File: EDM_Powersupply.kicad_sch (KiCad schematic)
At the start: 19 parts, among them Q1 IPW65R037C6, U1 L7805, U2 STGAP2SM, U3 RP2040, U4 L7815

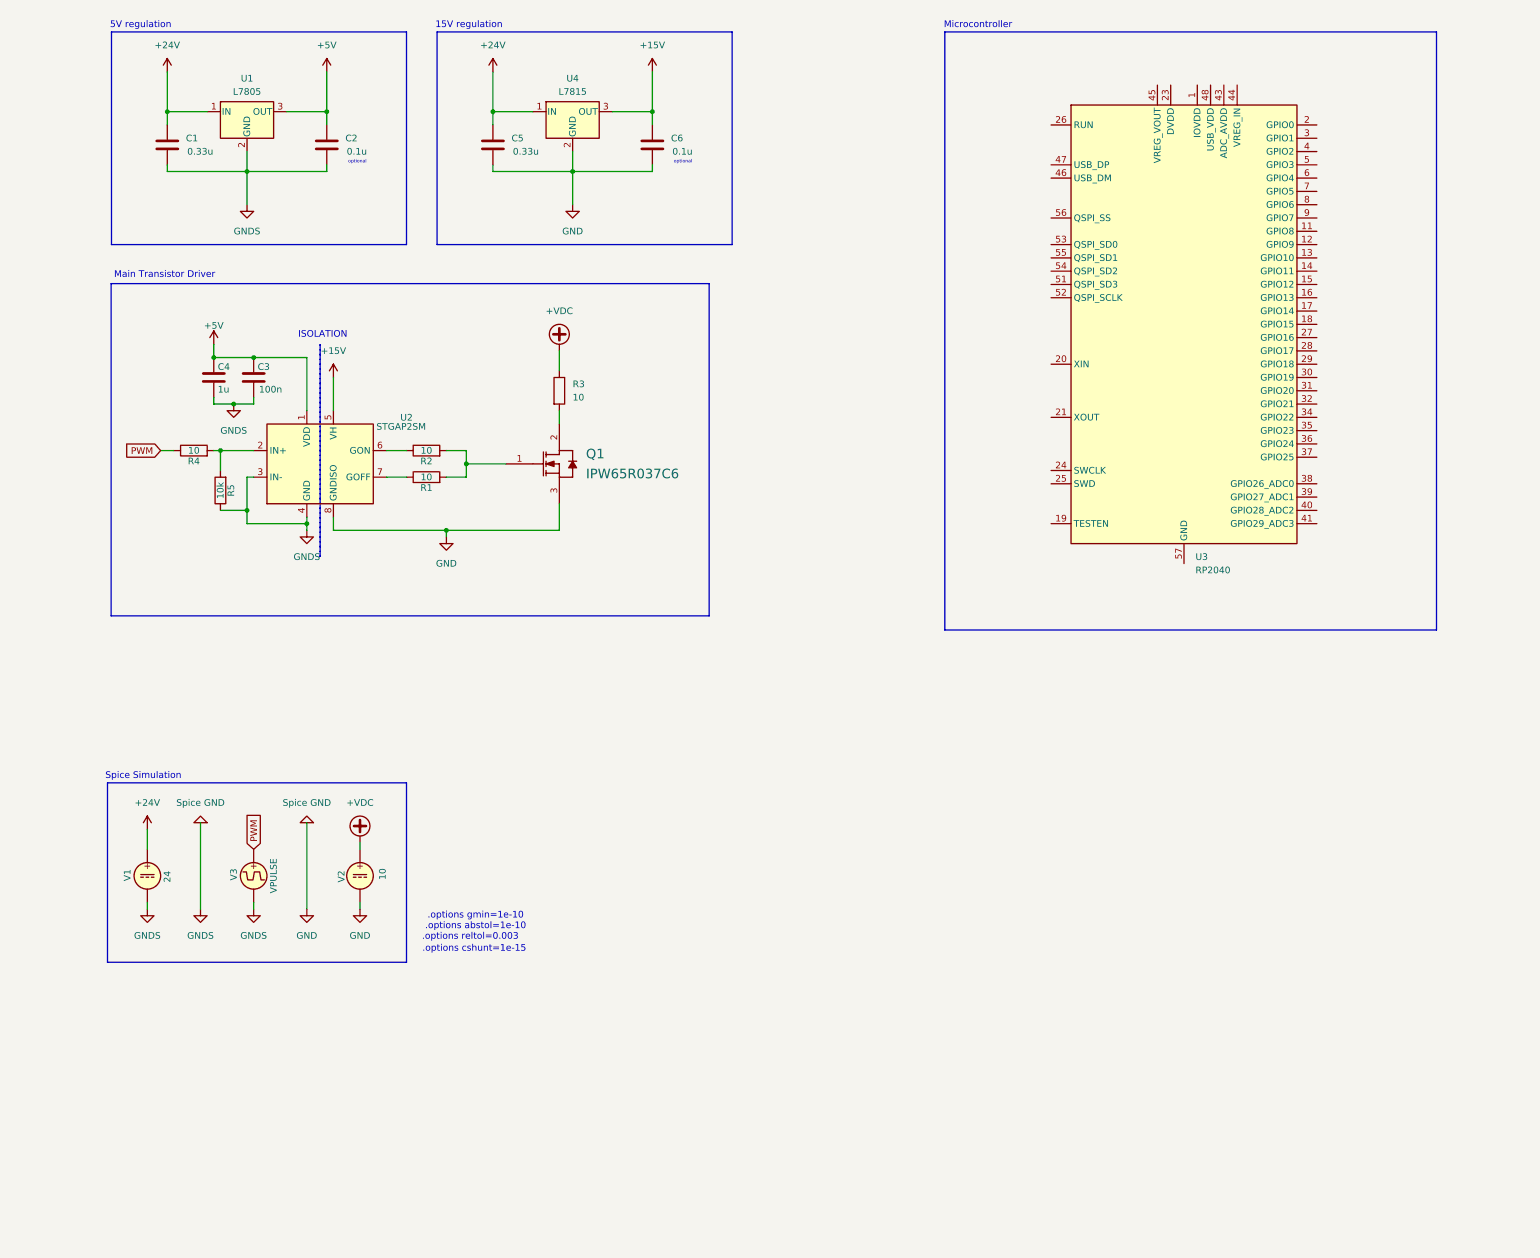
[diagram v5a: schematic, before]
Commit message: microcontroller support
microcontroller with voltage devider for analog and digital
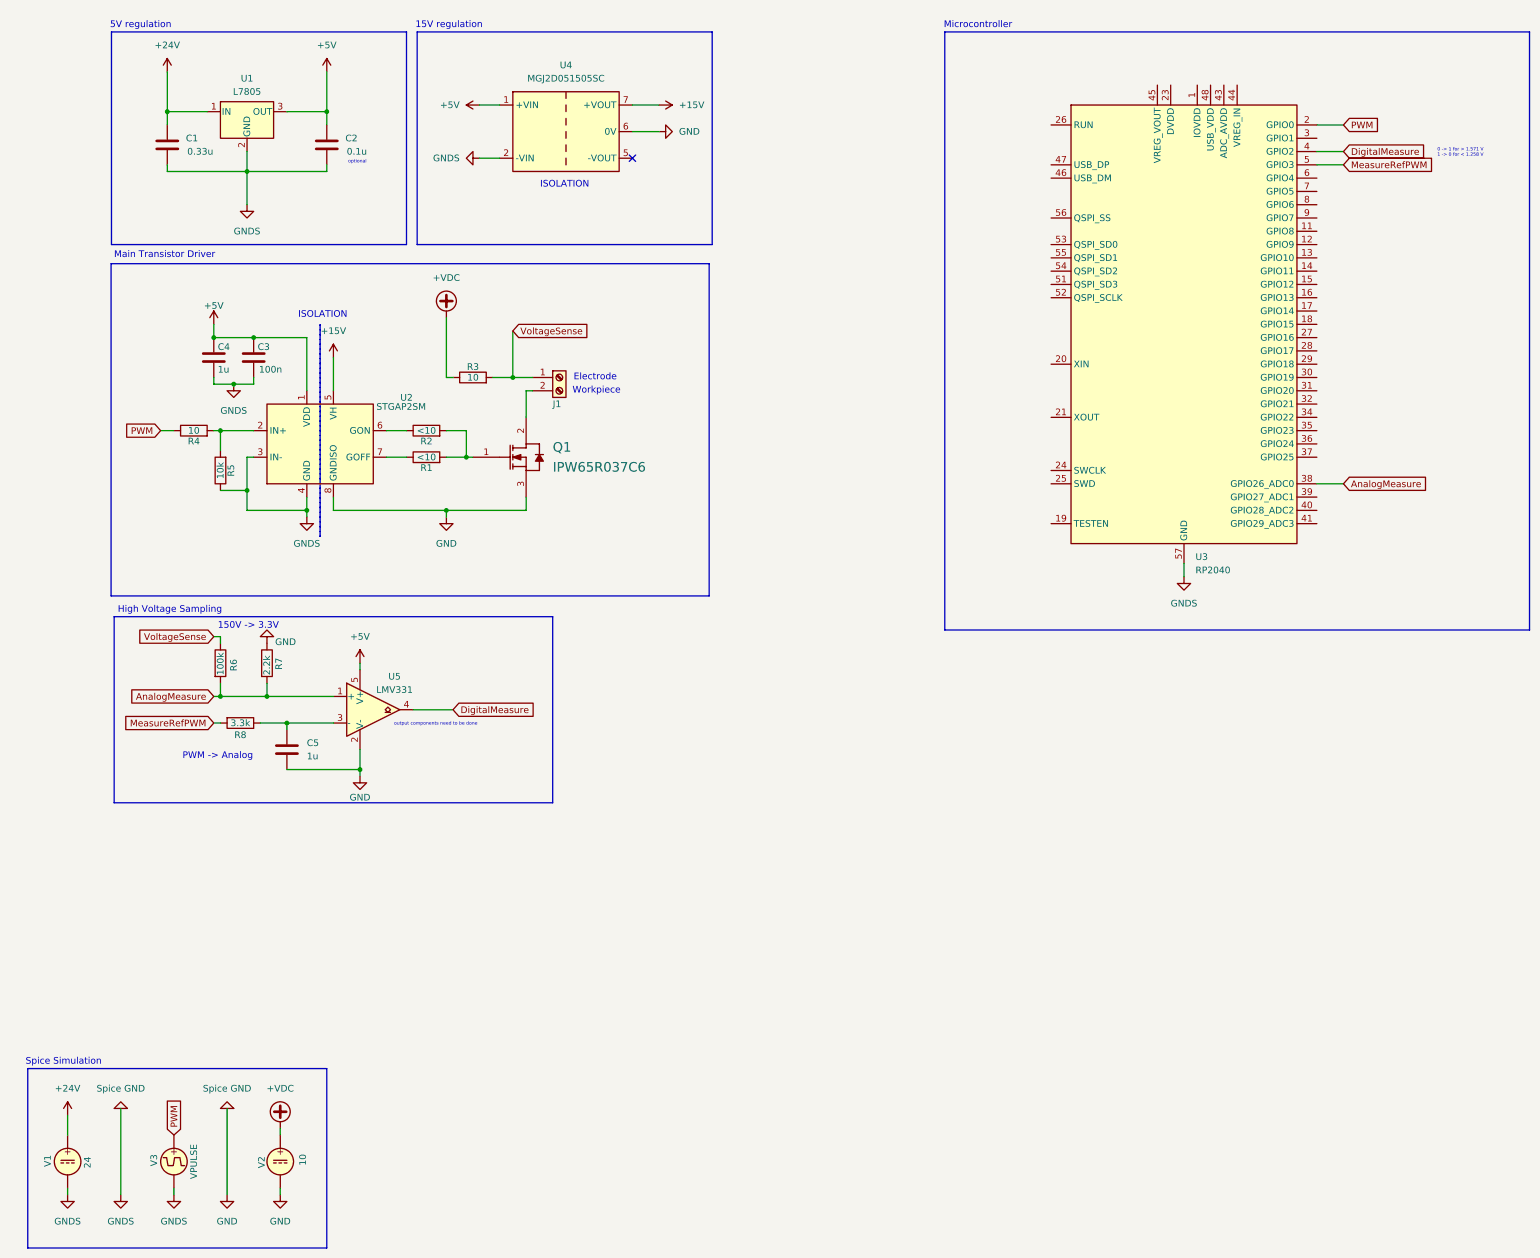
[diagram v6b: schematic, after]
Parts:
- removed C6: 0.1u, symbol Device:C
- removed U4: L7815, symbol Regulator_Linear:L7815
- added J1: Screw_Terminal_01x02, symbol Connector:Screw_Terminal_01x02
- added R6: 100k, symbol Device:R
- added R7: 2.2k, symbol Device:R
- added R8: 3.3k, symbol Device:R
- added U4: MGJ2D051505SC, Converter_DCDC:Converter_DCDC_Murata_MGJ2DxxxxxxSC_THT, symbol Converter_DCDC:MGJ2D051505SC
- added U5: LMV331, symbol Comparator:LMV331
- C5: value 0.33u -> 1u
- R1, R2: value 10 -> <10
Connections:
- net +15V: now also U4.7 (+VOUT)
- net +24V: no longer C5.1
- net +5V: now also U4.1 (+VIN), U5.5 (V+)
- net GND: now also U3.57 (GND), R7.1, U4.2 (-VIN), U4.6 (0V), U5.2 (V-)
- net PWM: now also U3.2 (GPIO0)
- net at Q1.2 (DRAIN): now also J1.2 (Pin_2); no longer R3.2
- net AnalogMeasure: now reaches U3.38 (GPIO26_ADC0)
- net AnalogMeasure: now also R6.2, R7.2, U5.1 (+)
- net DigitalMeasure: now reaches U3.4 (GPIO2)
- net DigitalMeasure: now also U5.4
- net MeasureRefPWM: now reaches U3.5 (GPIO3)
- net MeasureRefPWM: now also R8.2
- new net: C5.1, R8.1, U5.3 (-)
- new net VoltageSense: J1.1 (Pin_1), R3.2, R6.1
- no-connect marks 0 -> 1
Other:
- note added: "0 -> 1 for > 1.571 V 1 -> 0 for < 1.258 V"
- note added: "150V -> 3.3V"
- note added: "Electrode"
- note added: "High Voltage Sampling"
- note added: "PWM -> Analog"
- note added: "Workpiece"
- note added: "output components need to be done"
- note removed: ".options abstol=1e-10"
- note removed: ".options cshunt=1e-15"
- note removed: ".options gmin=1e-10"
- note removed: ".options reltol=0.003"
- moved on the sheet: C3, C4, Q1, R1, R2, R4, R5, U2, V1, V2, V3

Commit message: Signal isolation concept
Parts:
- added R10: 6.2k, symbol Device:R
- added R9: 22k, symbol Device:R
- added U6: ISO7320FC, Package_SO:SOIC-8_3.9x4.9mm_P1.27mm, symbol Isolator:ISO7320FC
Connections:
- net +15V: now also R9.1
- net GND: now also R10.2, U6.4 (GND1), U6.5 (GND2)
- net MeasureRefPWM: now also U6.7 (OUTA); no longer U3.5 (GPIO3)
- new net: R10.1, R9.2, U6.8 (VCC2)
- new net +3.3V: U6.1 (VCC1)
- new net MeasSigRefPWM: U3.5 (GPIO3), U6.2 (INA)
- no-connect marks 1 -> 3
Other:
- note added: "15V -> 3.3V"
- note added: "High side"
- note added: "Microcontroller PWM"

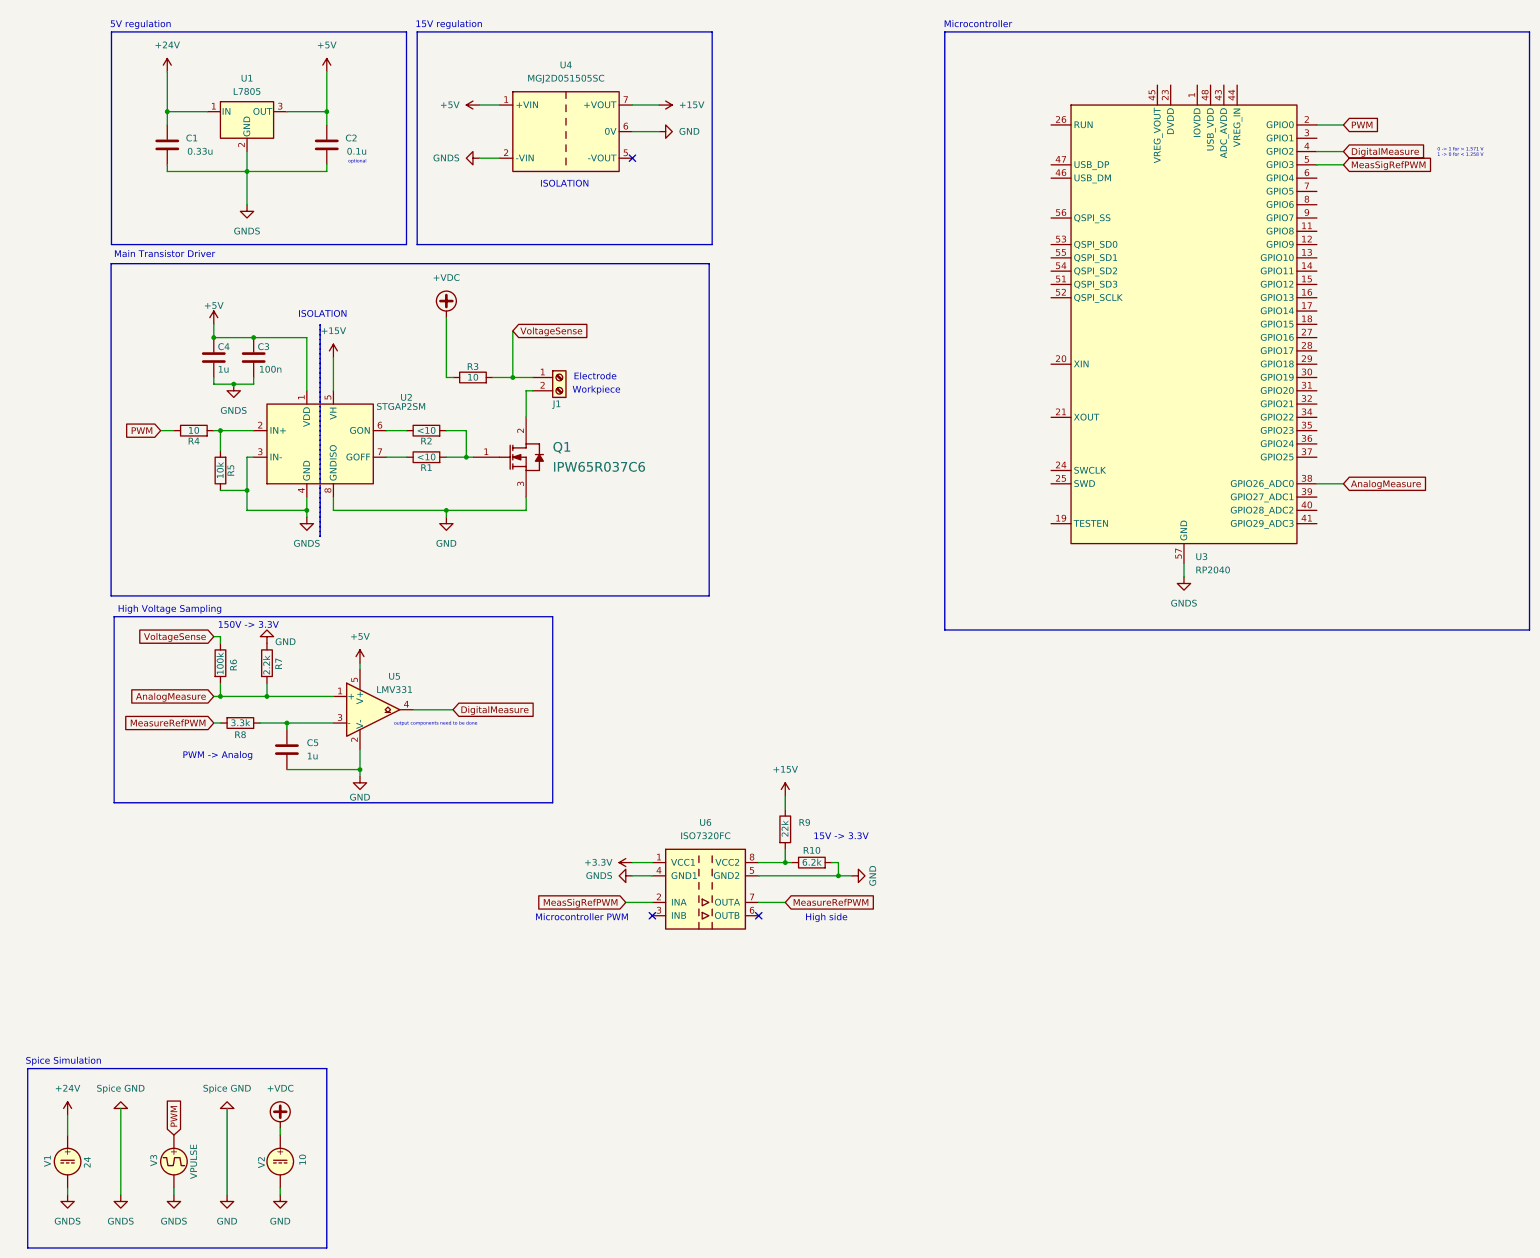
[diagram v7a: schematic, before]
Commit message: changed to high side switching
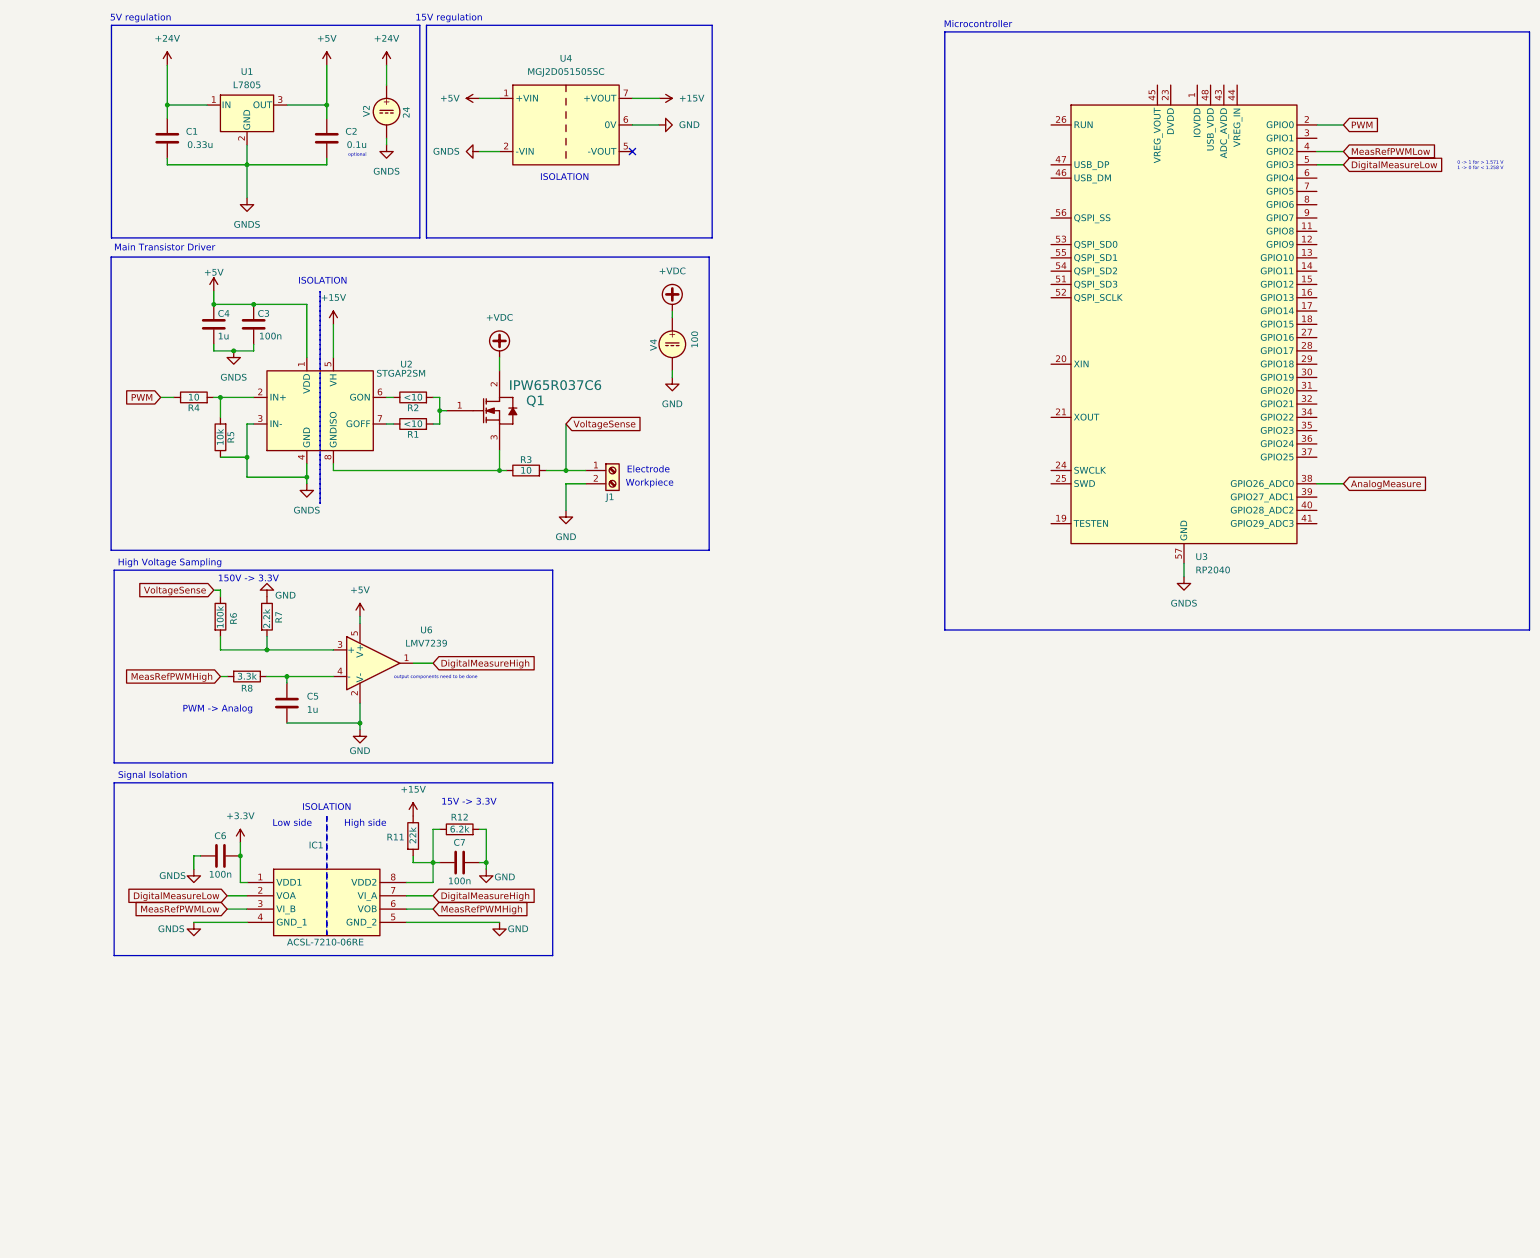
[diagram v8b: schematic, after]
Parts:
- removed R10: 6.2k, symbol Device:R
- removed R9: 22k, symbol Device:R
- removed U5: LMV331, symbol Comparator:LMV331
- removed U6: ISO7320FC, Package_SO:SOIC-8_3.9x4.9mm_P1.27mm, symbol Isolator:ISO7320FC
- removed V1: 24, symbol Simulation_SPICE:VDC
- removed V3: VPULSE, symbol Simulation_SPICE:VPULSE
- added C6, C7: 100n, symbol Device:C
- added IC1: ACSL-7210-06RE, SOIC127P600X175-8N, symbol ACSL-7210-06RE:ACSL-7210-06RE
- added R11: 22k, symbol Device:R
- added R12: 6.2k, symbol Device:R
- added U6: LMV7239, Package_TO_SOT_SMD:SOT-353_SC-70-5, symbol Comparator:LMV7219M7
- added V4: 100, symbol Simulation_SPICE:VDC
- V2: value 10 -> 24
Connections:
- net +15V: now also R11.1
- net +24V: now also V2.1
- net +3.3V: now also C6.2, IC1.1 (VDD1)
- net +5V: now also U6.5 (V+)
- net +VDC: now also Q1.2 (DRAIN), V4.1; no longer R3.1, V2.1
- net AnalogMeasure: no longer R6.2, R7.2
- net GND: now also J1.2 (Pin_2), C7.2, IC1.5 (GND_2), R12.2, U6.2 (V-), V4.2; no longer C1.2, C2.2, C3.2, C4.2, Q1.3 (SOURCE), R5.1, U1.2 (GND), U2.3 (IN-), U2.4 (GND), U2.8 (GNDISO), U3.57 (GND), U4.2 (-VIN), V2.2
- net at C5.1, R8.1: now also U6.4 (-)
- net DigitalMeasure renamed MeasRefPWMLow
- net MeasRefPWMLow: now also IC1.3 (VI_B)
- net MeasSigRefPWM renamed DigitalMeasureLow
- net DigitalMeasureLow: now also IC1.2 (VOA)
- net MeasureRefPWM renamed MeasRefPWMHigh
- net MeasRefPWMHigh: now also IC1.6 (VOB)
- new net: C7.1, IC1.8 (VDD2), R11.2, R12.1
- new net: R6.2, R7.2, U6.3 (+)
- new net: Q1.3 (SOURCE), R3.1, U2.8 (GNDISO)
- new net DigitalMeasureHigh: IC1.7 (VI_A), U6.1
- new net GNDS: C1.2, C2.2, C3.2, C4.2, C6.1, IC1.4 (GND_1), R5.1, U1.2 (GND), U2.3 (IN-), U2.4 (GND), U3.57 (GND), U4.2 (-VIN), V2.2
- no-connect marks 3 -> 1
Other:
- note added: "Low side"
- note added: "Signal Isolation"
- note removed: "Microcontroller PWM"
- note removed: "Spice Simulation"
- moved on the sheet: C1, C2, C3, C4, C5, J1, Q1, R1, R2, R3, R4, R5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
